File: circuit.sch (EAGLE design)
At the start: 13 parts, among them IC1 LM324N, IC2 LM324N

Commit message: Updated to use comparator instead of op amps
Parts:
- removed IC2: LM324N, linear:LM324N
- added IC3: LM339N, linear:LM339N
- added R10, R8, R9: 10k, rcl:R-US_0207/10
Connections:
- net +5V: now also IC3P.V+, R10.1, R8.1, R9.1; no longer IC2P.V+
- net GND: now also IC3P.GND; no longer IC2P.V-
- net N$10: now also IC3D.OUT, R8.2; no longer IC2C.OUT
- net N$11: now also IC3B.OUT, R9.2; no longer IC2A.OUT
- net N$12: now also IC3A.OUT, R10.2; no longer IC2B.OUT
- net N$13: now also IC3D.+IN; no longer IC2C.+IN
- net N$14: now also IC3B.+IN; no longer IC2A.+IN
- net N$15: now also IC3A.+IN; no longer IC2B.+IN
- net N$6: now also IC3A.-IN, IC3B.-IN, IC3D.-IN; no longer IC2A.-IN, IC2B.-IN, IC2C.-IN
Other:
- moved on the sheet: SV1, SV2

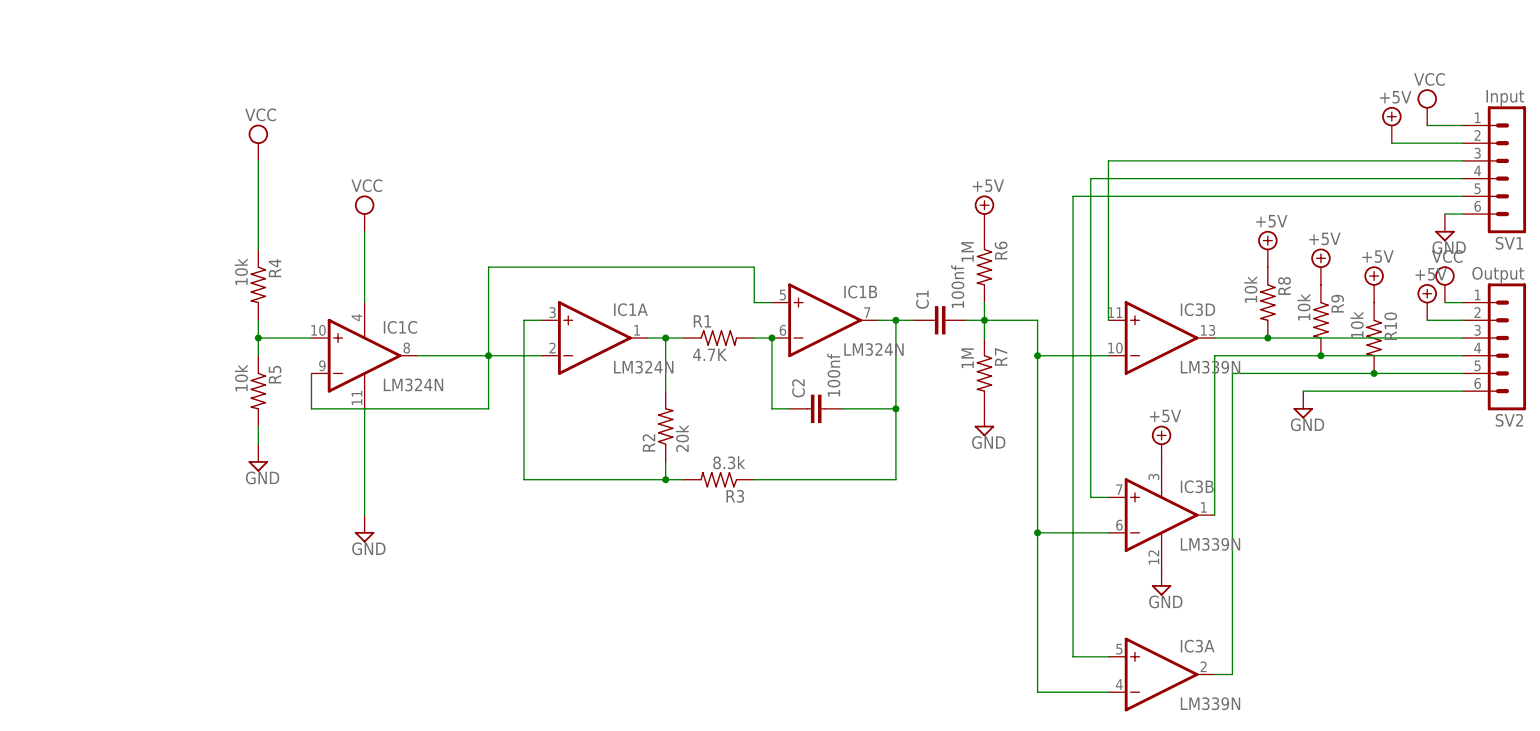
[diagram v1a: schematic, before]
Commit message: schematic: added decoupling caps for each IC as well as zener diodes so that the amplitude of the triangle wave is not dependent on supply voltage. Also added a trimpot to allow for triangle wave adjustment. board: redid board with ground plane
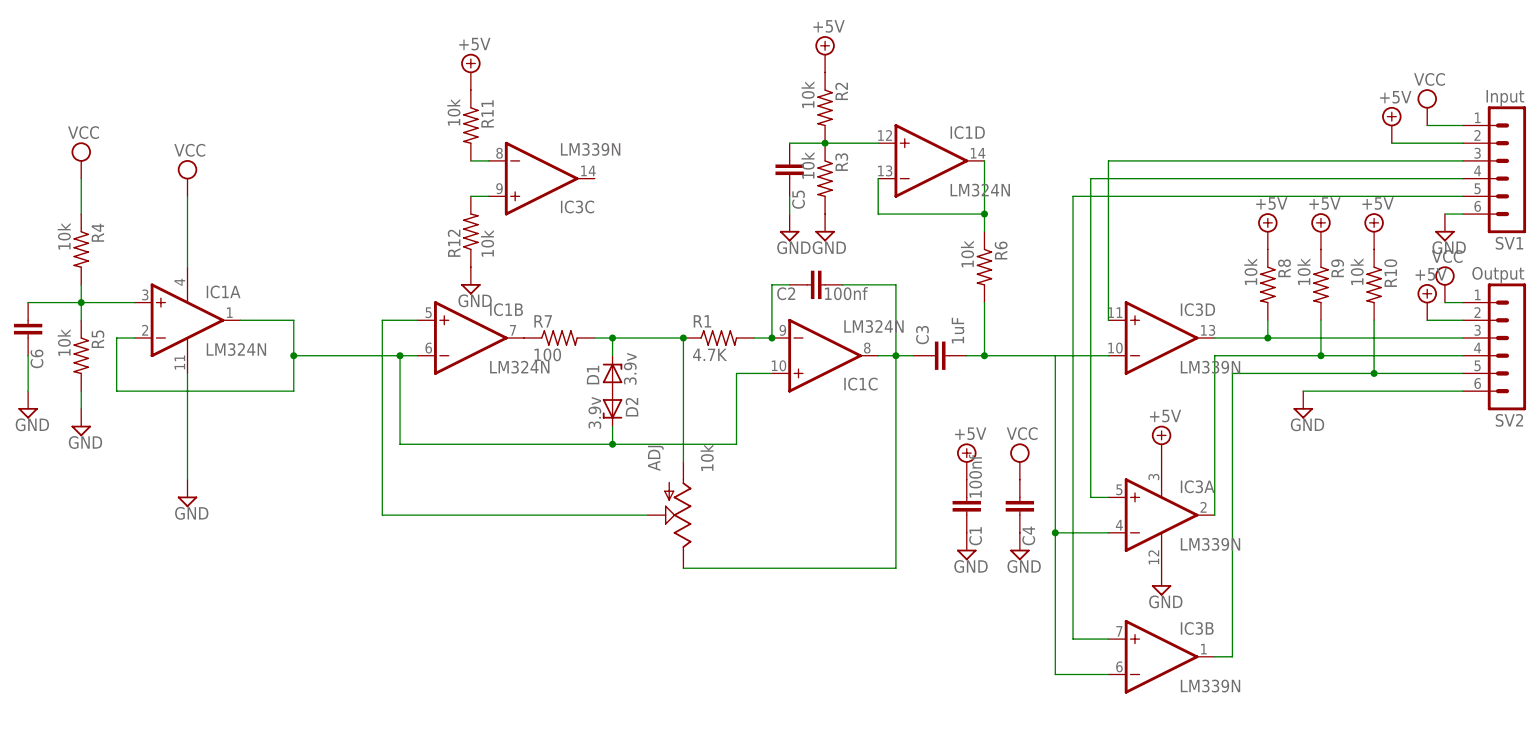
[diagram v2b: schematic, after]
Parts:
- added ADJ: 10k, SparkFun-Electromechanical:POTTRIM
- added C3: 1uF, resistor:C-EU050-035X075
- added C4, C5, C6: 100nf, rcl:C-EU050-024X044
- added D1, D2: 3.9v, diode:ZENER-DIODEDO41Z10
- added R11, R12: 10k, rcl:R-US_0207/10
- C1, C2: device rcl:C-EU025-025X050 -> rcl:C-EU050-024X044
- R1: device rcl:R-US_0207/10 -> rcl:R-US_0207/12
- R2: value 20k -> 10k
- R3: value 8.3k -> 10k
- R6: value 1M -> 10k
- R7: value 1M -> 100
- R8: device rcl:R-US_0207/10 -> rcl:R-US_0207/7
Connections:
- removed net N$6: C1.2, IC3A.-IN, IC3B.-IN, IC3D.-IN, R6.2, R7.1
- new net ARTGND: D2.C, IC1A.-IN, IC1A.OUT, IC1B.-IN, IC1C.+IN
- new net N$16: C5.2, IC1D.+IN, R2.2, R3.1
- new net N$17: IC3C.-IN, R11.2
- new net N$18: IC3C.+IN, R12.2
- new net N$19: C3.2, IC3A.-IN, IC3B.-IN, IC3D.-IN, R6.2
- new net N$5: IC1D.-IN, IC1D.OUT, R6.1
- new net N$7: ADJ.A, D1.C, R1.1, R7.2
- net +5V: now also C1.2, R11.1, R2.1; no longer R6.1
- net GND: now also C1.1, C4.1, C5.1, C6.1, R12.1, R3.2; no longer R7.2
- net N$1: now also ADJ.E, C3.1, IC1C.OUT; no longer C1.1, IC1B.OUT, R3.1
- net N$11: now also IC3A.OUT; no longer IC3B.OUT
- net N$12: now also IC3B.OUT; no longer IC3A.OUT
- net N$14: now also IC3A.+IN; no longer IC3B.+IN
- net N$15: now also IC3B.+IN; no longer IC3A.+IN
- net N$2: now also IC1B.OUT, R7.1; no longer IC1A.-IN, IC1B.+IN, IC1C.-IN, IC1C.OUT
- net N$3: now also D1.A, D2.A; no longer IC1A.OUT, R1.1, R2.2
- net N$4: now also IC1C.-IN; no longer IC1B.-IN
- net N$8: now also C6.2, IC1A.+IN; no longer IC1C.+IN
- net N$9: now also ADJ.S, IC1B.+IN; no longer IC1A.+IN, R2.1, R3.2
- net VCC: now also C4.2
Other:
- moved on the sheet: C1, C2, IC1A, IC1B, IC1C, IC3A, IC3B, R10, R2, R3, R4, R5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
